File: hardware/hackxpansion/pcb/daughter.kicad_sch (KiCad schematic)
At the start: 4 parts

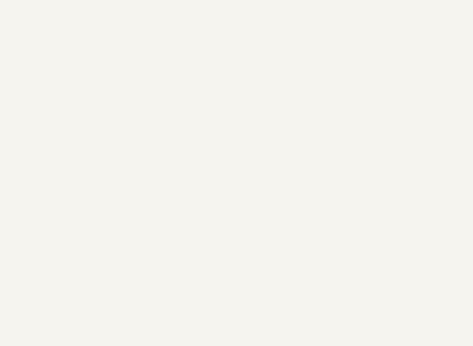
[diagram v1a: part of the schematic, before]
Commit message: added silkscreen
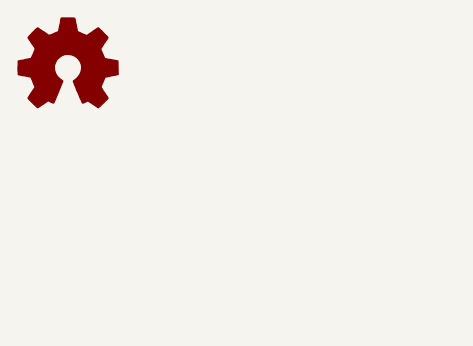
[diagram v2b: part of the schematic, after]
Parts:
- added SYM2: Logo_Open_Hardware_Small, Symbol:OSHW-Logo_5.7x6mm_SilkScreen, symbol Graphic:Logo_Open_Hardware_Small
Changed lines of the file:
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@@
+	)
+	(symbol
+		(lib_id "Graphic:Logo_Open_Hardware_Small")
+		(at 20.32 19.05 0)
+		(unit 1)
+		(body_style 1)
+		(exclude_from_sim no)
+		(in_bom no)
+		(on_board yes)
+		(in_pos_files yes)
+		(dnp no)
+		(fields_autoplaced yes)
+		(property "Reference" "SYM2"
+			(at 20.32 12.065 0)
+			(hide yes)
+			(show_name no)
+			(do_not_autoplace no)
+			(effects
+				(font
+					(size 1.27 1.27)
+				)
+			)
+		)
+		(property "Value" "Logo_Open_Hardware_Small"
+			(at 20.32 24.765 0)
+			(hide yes)
+			(show_name no)
+			(do_not_autoplace no)
+			(effects
+				(font
+					(size 1.27 1.27)
+				)
+			)
+		)
+		(property "Footprint" "Symbol:OSHW-Logo_5.7x6mm_SilkScreen"
+			(at 20.32 19.05 0)
+			(hide yes)
+			(show_name no)
+			(do_not_autoplace no)
+			(effects
+				(font
+					(size 1.27 1.27)
+				)
+			)
+		)
+		(property "Datasheet" ""
+			(at 20.32 19.05 0)
+			(hide yes)
+			(show_name no)
+			(do_not_autoplace no)
+			(effects
+				(font
+					(size 1.27 1.27)
+				)
+			)
+		)
+		(property "Description" "Open Hardware logo, small"
+			(at 20.32 19.05 0)
+			(hide yes)
+			(show_name no)
+			(do_not_autoplace no)
+			(effects
+				(font
+					(size 1.27 1.27)
+				)
+			)
+		)
+		(property "Sim.Enable" "0"
+			(at 20.32 19.05 0)
+			(hide yes)
+			(show_name no)
+			(do_not_autoplace no)
+			(effects
+				(font
+					(size 1.27 1.27)
+				)
+			)
+		)
+		(instances
+			(project "hackxpansion"
+				(path "/aaf5804d-3f78-442b-969e-39faa388db94/7b3174ee-89a2-4fc3-aea9-d162748ee587"
+					(reference "SYM2")
+					(unit 1)
+				)
+			)
+		)
 	)
 	(symbol
